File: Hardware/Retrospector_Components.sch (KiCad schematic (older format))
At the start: 122 parts, among them J1 SWD_Header, J2 Eurorack_10_pin_power, J3 Conn_01x08_Male, J4 Conn_01x08_Male, J5 Conn_01x08_Male, J6 Conn_01x08_Male, J7 USB_B_Micro, U1 STM32H743ZITx, U2 IS42S16400J-xC, U3 PCM5100APW, U4 SSI2164, U5 MCP6004, U6 MCP6004, U7 TL074, U8 LM1117-3.3, Y1 8MHz 20pF

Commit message: Final changes to PCBs for manufacture
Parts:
- added C53: 10uF, Capacitors_SMD:C_0805, symbol Device:C_Small
- C31, C33, C4, C6: footprint Capacitors_SMD:C_0805 -> Capacitors_SMD:C_0603_HandSoldering; Part_Number C49217 -> C23630
- C36: Rotation (none) -> 270
- C39, C40: footprint Capacitors_SMD:CP_Elec_5x5.3 -> Capacitors_SMD:CP_Elec_6.3x5.3; Part_Number (none) -> C249771
- C41: footprint Capacitors_SMD:CP_Elec_5x5.3 -> Capacitors_SMD:CP_Elec_6.3x7.7; Part_Number C134798 -> C108053; Rotation (none) -> 270
- D2, U8: Rotation (none) -> 90
- U1, U3: Rotation (none) -> 180
- Y1: footprint Crystals:Crystal_SMD_0603-2pin_6.0x3.5mm_HandSoldering -> Crystals:Crystal_SMD_5032-2pin_5.0x3.2mm_HandSoldering; Part_Number (none) -> C115962
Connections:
- wire segments 581 -> 584
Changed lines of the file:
@@
 F 3 "http://www.ti.com/lit/ds/symlink/lm4040-n.pdf" H 4050 11850 50  0001 C CIN
 F 4 "C69316" H 4050 11850 50  0001 C CNN "Part_Number"
+F 5 "90" H 4050 11850 50  0001 C CNN "Rotation"
 	1    4050 11850
 	0    1    1    0
@@
 F 0 "C41" H 4750 10250 50  0000 C CNN
 F 1 "47uF" H 4750 10150 50  0000 C CNN
-F 2 "Capacitors_SMD:CP_Elec_5x5.3" H 4588 10100 50  0001 C CNN
+F 2 "Capacitors_SMD:CP_Elec_6.3x7.7" H 4588 10100 50  0001 C CNN
 F 3 "~" H 4550 10250 50  0001 C CNN
-F 4 "C134798" H 4550 10250 50  0001 C CNN "Part_Number"
+F 4 "C108053" H 4550 10250 50  0001 C CNN "Part_Number"
+F 5 "270" H 4550 10250 50  0001 C CNN "Rotation"
 	1    4550 10250
 	1    0    0    -1
@@
 F 3 "http://ww1.microchip.com/downloads/en/DeviceDoc/21733j.pdf" H 9850 2150 50  0001 C CNN
 F 4 "C7378" H 9800 1950 50  0001 C CNN "Part_Number"
+F 5 "" H 9800 1950 50  0001 C CNN "Rotation"
 	1    9800 1950
 	1    0    0    1
@@
 F 0 "C39" V 1795 10000 50  0000 C CNN
 F 1 "22uF" V 1886 10000 50  0000 C CNN
-F 2 "Capacitors_SMD:CP_Elec_5x5.3" H 2088 9850 50  0001 C CNN
+F 2 "Capacitors_SMD:CP_Elec_6.3x5.3" H 2088 9850 50  0001 C CNN
 F 3 "~" H 2050 10000 50  0001 C CNN
-F 4 "" H 2050 10000 50  0001 C CNN "Part_Number"
+F 4 "C249771" H 2050 10000 50  0001 C CNN "Part_Number"
 	1    2050 10000
 	0    1    1    0
@@
 F 0 "C40" V 2305 11300 50  0000 C CNN
 F 1 "22uF" V 2214 11300 50  0000 C CNN
-F 2 "Capacitors_SMD:CP_Elec_5x5.3" H 2088 11150 50  0001 C CNN
+F 2 "Capacitors_SMD:CP_Elec_6.3x5.3" H 2088 11150 50  0001 C CNN
 F 3 "~" H 2050 11300 50  0001 C CNN
-F 4 "" H 2050 11300 50  0001 C CNN "Part_Number"
+F 4 "C249771" H 2050 11300 50  0001 C CNN "Part_Number"
 	1    2050 11300
 	0    -1   -1   0
@@
 F 3 "http://www.ti.com/lit/ds/symlink/lm1117.pdf" H 4050 10050 50  0001 C CNN
 F 4 "C6186" H 4050 10050 50  0001 C CNN "Part_Number"
+F 5 "90" H 4050 10050 50  0001 C CNN "Rotation"
 	1    4050 10050
 	1    0    0    -1
@@
 F 3 "https://lcsc.com/product-detail/Aluminum-Electrolytic-Capacitors-SMD_Lelon-VE-100M1HTR-0505_C249452.html/?href=jlc-SMT" H 3650 10250 50  0001 C CNN
 F 4 "C249452" H 3650 10250 50  0001 C CNN "Part_Number"
+F 5 "270" H 3650 10250 50  0001 C CNN "Rotation"
 	1    3650 10250
 	1    0    0    -1
@@
 F 0 "C6" V 1450 2350 50  0000 C CNN
 F 1 "2.2uF" V 1450 2600 50  0000 C CNN
-F 2 "Capacitors_SMD:C_0805" H 1500 2450 50  0001 C CNN
+F 2 "Capacitors_SMD:C_0603_HandSoldering" H 1500 2450 50  0001 C CNN
 F 3 "~" H 1500 2450 50  0001 C CNN
-F 4 "C49217" H 1500 2450 50  0001 C CNN "Part_Number"
+F 4 "C23630" H 1500 2450 50  0001 C CNN "Part_Number"
 	1    1500 2450
 	0    1    1    0
@@
 F 0 "C4" V 1250 2450 50  0000 C CNN
 F 1 "2.2uF" V 1250 2700 50  0000 C CNN
-F 2 "Capacitors_SMD:C_0805" H 1200 2550 50  0001 C CNN
+F 2 "Capacitors_SMD:C_0603_HandSoldering" H 1200 2550 50  0001 C CNN
 F 3 "~" H 1200 2550 50  0001 C CNN
-F 4 "C49217" H 1200 2550 50  0001 C CNN "Part_Number"
+F 4 "C23630" H 1200 2550 50  0001 C CNN "Part_Number"
 	1    1200 2550
 	0    1    1    0
@@
 F 0 "Y1" V 1600 3200 50  0000 R CNN
 F 1 "8MHz 20pF" V 1700 3400 50  0000 R CNN
-F 2 "Crystals:Crystal_SMD_0603-2pin_6.0x3.5mm_HandSoldering" H 1500 3300 50  0001 C CNN
+F 2 "Crystals:Crystal_SMD_5032-2pin_5.0x3.2mm_HandSoldering" H 1500 3300 50  0001 C CNN
 F 3 "~" H 1500 3300 50  0001 C CNN
+F 4 "C115962" H 1500 3300 50  0001 C CNN "Part_Number"
 	1    1500 3300
 	0    -1   -1   0
@@
 F 3 "http://www.ti.com/lit/ds/symlink/pcm5100.pdf" H 10450 10650 50  0001 C CNN
 F 4 "C131154" H 10500 9900 50  0001 C CNN "Part_Number"
+F 5 "180" H 10500 9900 50  0001 C CNN "Rotation"
 	1    10500 9900
 	1    0    0    -1
@@
 F 0 "C33" H 11265 10596 50  0000 L CNN
 F 1 "2.2uF" H 11265 10505 50  0000 L CNN
-F 2 "Capacitors_SMD:C_0805" H 11188 10400 50  0001 C CNN
+F 2 "Capacitors_SMD:C_0603_HandSoldering" H 11188 10400 50  0001 C CNN
 F 3 "~" H 11150 10550 50  0001 C CNN
-F 4 "C49217" H 11150 10550 50  0001 C CNN "Part_Number"
+F 4 "C23630" H 11150 10550 50  0001 C CNN "Part_Number"
 	1    11150 10550
 	1    0    0    -1
@@
 F 0 "C31" H 11265 9996 50  0000 L CNN
 F 1 "2.2uF" H 11265 9905 50  0000 L CNN
-F 2 "Capacitors_SMD:C_0805" H 11188 9800 50  0001 C CNN
+F 2 "Capacitors_SMD:C_0603_HandSoldering" H 11188 9800 50  0001 C CNN
 F 3 "~" H 11150 9950 50  0001 C CNN
-F 4 "C49217" H 11150 9950 50  0001 C CNN "Part_Number"
+F 4 "C23630" H 11150 9950 50  0001 C CNN "Part_Number"
 	1    11150 9950
 	1    0    0    -1
@@
 F 3 "http://www.st.com/st-web-ui/static/active/en/resource/technical/document/datasheet/DM00387108.pdf" H 3050 5250 50  0001 C CNN
 F 4 "C114408" H 3050 5250 50  0001 C CNN "Part_Number"
+F 5 "180" H 3050 5250 50  0001 C CNN "Rotation"
 	1    3050 5250
 	1    0    0    -1
@@
 	1    0    0    -1
 $EndComp
+$Comp
+L Device:C_Small C53
+U 1 1 5F91DB5F
+P 6050 10050
+F 0 "C53" H 5850 10150 50  0000 L CNN
+F 1 "10uF" H 5800 9950 50  0000 L CNN
+F 2 "Capacitors_SMD:C_0805" H 6088 9900 50  0001 C CNN
+F 3 "~" H 6050 10050 50  0001 C CNN
+F 4 "C15850 " H 6050 10050 50  0001 C CNN "Part_Number"
+	1    6050 10050
+	1    0    0    -1
+$EndComp
+Wire Wire Line
+	6050 9950 6250 9950
+Connection ~ 6250 9950
+Wire Wire Line
+	6050 10150 6050 10550
+Wire Wire Line
+	6050 10550 6250 10550
+Connection ~ 6250 10550
 $EndSCHEMATC

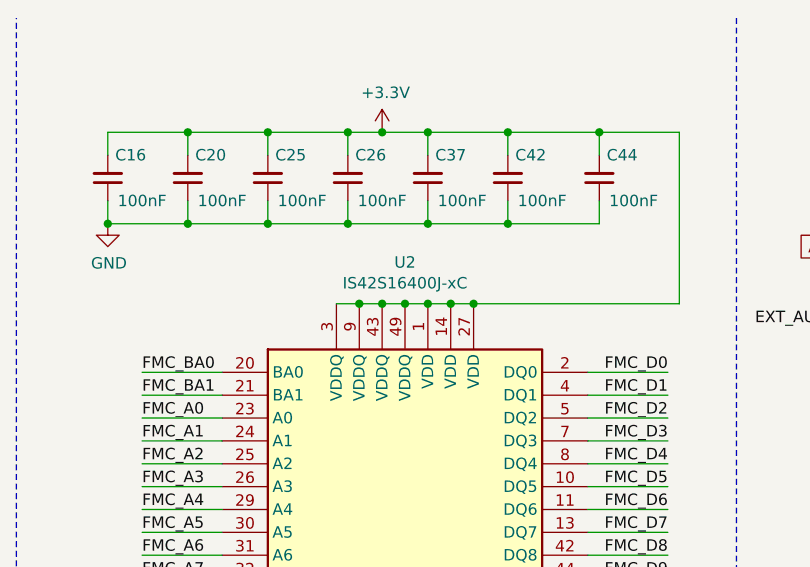
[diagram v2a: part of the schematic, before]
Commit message: Reduced clock speed; started implementing SDRAM code; ADC updates
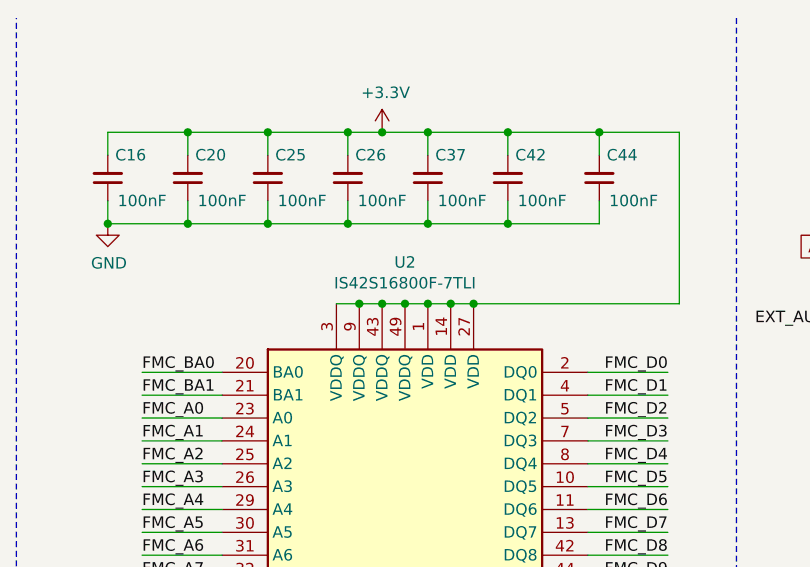
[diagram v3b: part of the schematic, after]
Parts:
- U2: value IS42S16400J-xC -> IS42S16800F-7TLI
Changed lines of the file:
@@
 P 6950 3150
 F 0 "U2" H 6950 4731 50  0000 C CNN
-F 1 "IS42S16400J-xC" H 6950 4640 50  0000 C CNN
+F 1 "IS42S16800F-7TLI" H 6950 4640 50  0000 C CNN
 F 2 "Custom_Footprints:TSOP-II-54_22.2x10.16mm_P0.8mm" H 6950 3150 50  0001 C CNN
-F 3 "http://www.issi.com/WW/pdf/42-45S16400J.pdf" H 6350 4400 50  0001 C CNN
+F 3 "https://lcsc.com/product-detail/DDR_ISSI-Integrated-Silicon-Solution-IS42S16800F-7TLI_C69411.html" H 6350 4400 50  0001 C CNN
 F 4 "C69411" H 6950 3150 50  0001 C CNN "Part_Number"
 	1    6950 3150

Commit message: Started updating schematics and pcb layout for rev 2 changes; updated and tested clock pin to use production assignment
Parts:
- removed C38: 100nF, Capacitors_SMD:C_0603_HandSoldering, symbol Device:C
- removed R22: 2k2, Resistors_SMD:R_0603_HandSoldering, symbol Device:R
- removed R42, R43: 1k, Resistors_SMD:R_0603_HandSoldering, symbol Device:R
- removed U8: LM1117-3.3, TO_SOT_Packages_SMD:SOT-223, symbol Regulator_Linear:LM1117-3.3
- added C38: 100nF, Capacitors_SMD:C_0603_HandSoldering, symbol Device:C_Small
- added C54, C55: 22uF, Capacitors_SMD:CP_Elec_4x5.8, symbol Device:C
- added C56: 10nF, Capacitors_SMD:C_0603_HandSoldering, symbol Device:C_Small
- added R22: 2k2, Resistors_SMD:R_0603_HandSoldering, symbol Device:R_Small
- added R43: 100R, Resistors_SMD:R_0603_HandSoldering, symbol Device:R_Small
- added TP? (x2): TestPoint, Custom_Footprints:1.3mm_Test_Point, symbol Connector:TestPoint
- added U8: NCV1117DT33T5G, TO_SOT_Packages_SMD:TO-252-2_Rectifier, symbol LDO_DPAK:NCV1117DT33T5G
- added U9: BA7807FP-E2, TO_SOT_Packages_SMD:TO-252-2_Rectifier, symbol LDO_DPAK:BA7807FP-E2
- C36: value 10uF -> 22uF; footprint Capacitors_SMD:CP_Elec_3x5.3 -> Capacitors_SMD:CP_Elec_4x5.8; Part_Number C249452 -> C178597; Rotation 270 -> (none)
- C39, C40: footprint Capacitors_SMD:CP_Elec_6.3x5.3 -> Capacitors_SMD:CP_Elec_4x5.8; Part_Number C249771 -> C178597
- C41: value 47uF -> 22uF; footprint Capacitors_SMD:CP_Elec_6.3x7.7 -> Capacitors_SMD:CP_Elec_4x5.8; Part_Number C108053 -> C178597; Rotation 270 -> (none)
- TP1, TP2, TP3, TP4, TP5, TP6: footprint Measurement_Points:Test_Point_Keystone_5005-5009_Compact -> Custom_Footprints:1.3mm_Test_Point
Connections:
- net labels added: +7V
- wire segments 584 -> 599
- no-connect marks 64 -> 63
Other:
- note added: "FIXME - resistors R42/43 are redundant??"
- moved on the sheet: C36, C39, C40, C41, C53, D2, D3, D4, J2, L1, TP1, TP2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

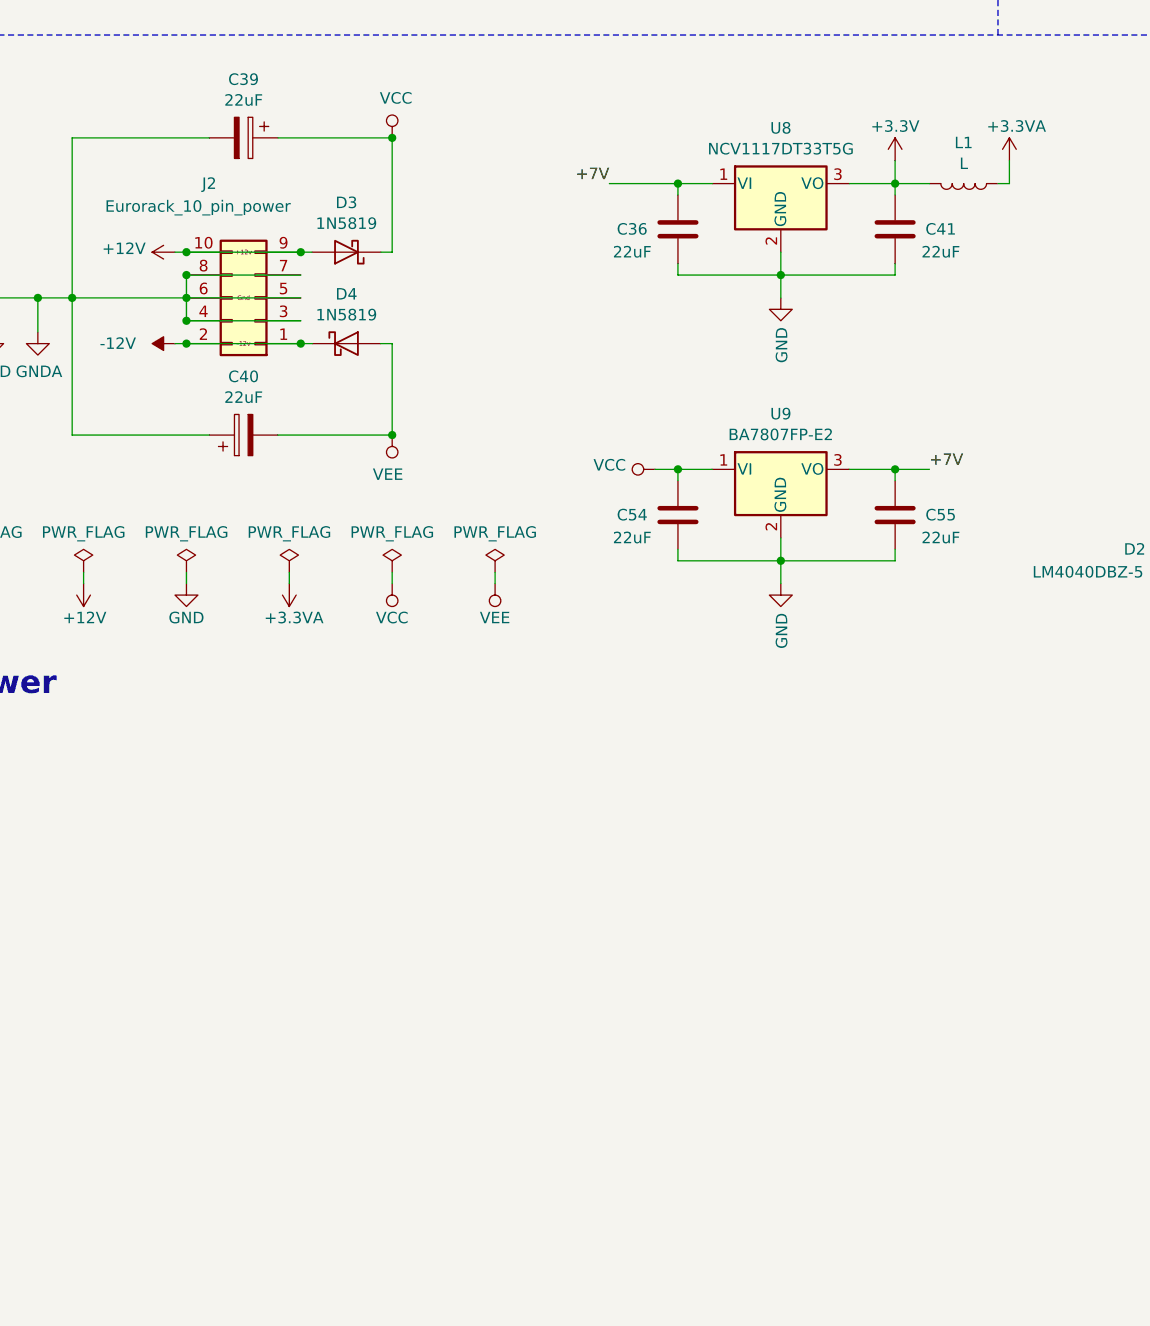
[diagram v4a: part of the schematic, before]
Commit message: Started adding circuitry for Buck conversion
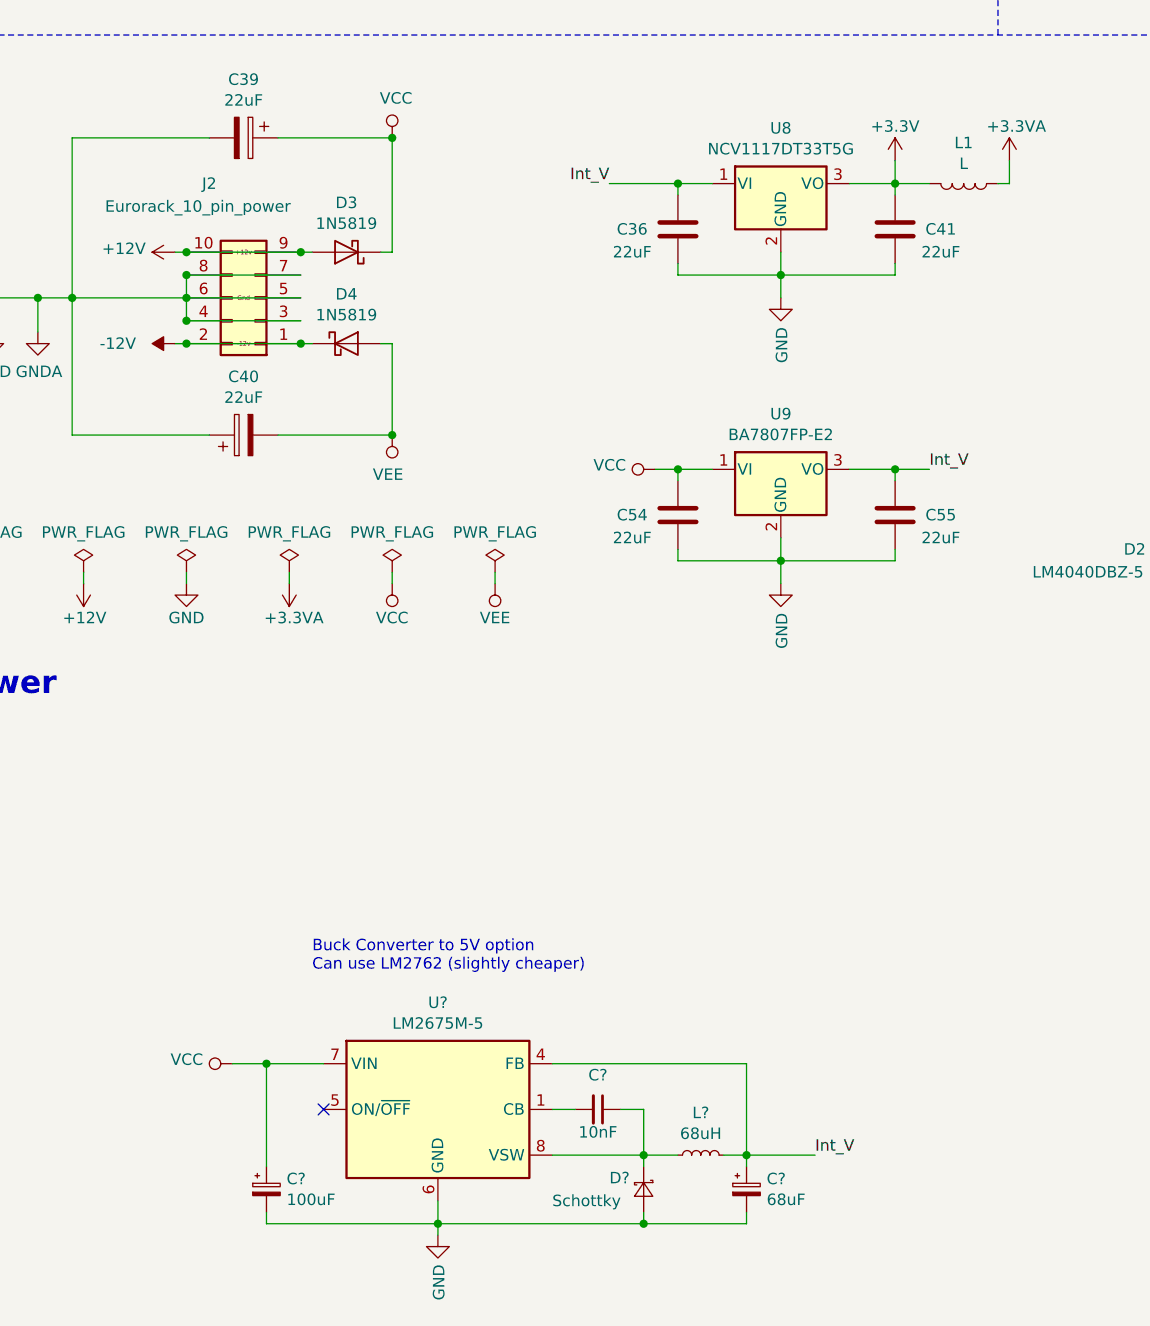
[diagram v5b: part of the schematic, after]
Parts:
- added C?: 10nF, Capacitors_SMD:C_0603_HandSoldering, symbol Device:C_Small
- added C?: 68uF, symbol Device:CP_Small
- added C?: 100uF, symbol Device:CP_Small
- added D?: Schottky, symbol Device:D_Schottky_Small
- added L?: 68uH, symbol Device:L_Small
- added U?: LM2675M-5, Housings_SOIC:SOIC-8_3.9x4.9mm_Pitch1.27mm, symbol Regulator_Switching:LM2675M-5
- C56: Part_Number (none) -> C57112
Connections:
- net GND: now also C?.2, C?.2, D?.2 (A), U?.6 (GND)
- net VCC: now also C?.1, U?.7 (VIN)
- net +7V renamed Int_V
- net Int_V: now also C?.1, L?.2, U?.4 (FB)
- new net: C?.2, U?.1 (CB)
- new net: C?.1, D?.1 (K), L?.1, U?.8 (VSW)
- no-connect marks 63 -> 64
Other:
- note added: "Buck Converter to 5V option\nCan use LM2762 (slightly cheaper)"
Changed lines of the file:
@@
 F 2 "Capacitors_SMD:C_0603_HandSoldering" H 14850 10500 50  0001 C CNN
 F 3 "~" H 14850 10500 50  0001 C CNN
-F 4 "" H 14850 10500 50  0001 C CNN "Part_Number"
+F 4 "C57112" H 14850 10500 50  0001 C CNN "Part_Number"
 	1    14850 10500
 	1    0    0    -1
@@
 Wire Wire Line
 	4300 11750 4800 11750
-Text Label 4950 11350 0    50   ~ 0
-+7V
-Text Label 3550 10100 2    50   ~ 0
-+7V
 Wire Wire Line
 	14050 10650 14050 10550
@@
 Wire Wire Line
 	7750 12250 7800 12250
+$Comp
+L Regulator_Switching:LM2675M-5 U?
+U 1 1 6DAC0E92
+P 2800 14150
+F 0 "U?" H 2800 14617 50  0000 C CNN
+F 1 "LM2675M-5" H 2800 14526 50  0000 C CNN
+F 2 "Housings_SOIC:SOIC-8_3.9x4.9mm_Pitch1.27mm" H 2850 13800 50  0001 L CIN
+F 3 "http://www.ti.com/lit/ds/symlink/lm2675.pdf" H 2800 14150 50  0001 C CNN
+F 4 "C180371" H 2800 14150 50  0001 C CNN "Part_Number"
+	1    2800 14150
+	1    0    0    -1
+$EndComp
+NoConn ~ 2300 14150
+$Comp
+L power:VCC #PWR?
+U 1 1 6DB2F14A
+P 1900 13950
+F 0 "#PWR?" H 1900 13800 50  0001 C CNN
+F 1 "VCC" V 1918 14077 50  0000 L CNN
+F 2 "" H 1900 13950 50  0001 C CNN
+F 3 "" H 1900 13950 50  0001 C CNN
+	1    1900 13950
+	0    -1   -1   0
+$EndComp
+$Comp
+L Device:D_Schottky_Small D?
+U 1 1 6DB2FC15
+P 3700 14500
+F 0 "D?" V 3650 14350 50  0000 L CNN
+F 1 "Schottky" V 3750 14100 50  0000 L CNN
+F 2 "" V 3700 14500 50  0001 C CNN
+F 3 "~" V 3700 14500 50  0001 C CNN
+	1    3700 14500
+	0    1    1    0
+$EndComp
+Wire Wire Line
+	3300 14350 3700 14350
+Wire Wire Line
+	3700 14350 3700 14400
+Wire Wire Line
+	2800 14550 2800 14650
+$Comp
+L Device:C_Small C?
+U 1 1 6DC7C12C
+P 3500 14150
+F 0 "C?" V 3350 14150 50  0000 C CNN
+F 1 "10nF" V 3600 14150 50  0000 C CNN
+F 2 "Capacitors_SMD:C_0603_HandSoldering" H 3500 14150 50  0001 C CNN
+F 3 "~" H 3500 14150 50  0001 C CNN
+F 4 "C57112" H 3500 14150 50  0001 C CNN "Part_Number"
+	1    3500 14150
+	0    1    1    0
+$EndComp
+Wire Wire Line
+	3300 14150 3400 14150
+Wire Wire Line
+	3600 14150 3700 14150
+Wire Wire Line
+	3700 14150 3700 14350
+Connection ~ 3700 14350
+$Comp
+L Device:CP_Small C?
+U 1 1 6DEA7A83
+P 4150 14500
+F 0 "C?" H 4238 14546 50  0000 L CNN
+F 1 "68uF" H 4238 14455 50  0000 L CNN
+F 2 "" H 4150 14500 50  0001 C CNN
+F 3 "~" H 4150 14500 50  0001 C CNN
+	1    4150 14500
+	1    0    0    -1
+$EndComp
+Wire Wire Line
+	3700 14350 3850 14350
+Wire Wire Line
+	4050 14350 4150 14350
+Wire Wire Line
+	4150 14350 4150 14400
+Wire Wire Line
+	4150 14650 4150 14600
+Connection ~ 2800 14650
+Wire Wire Line
+	2800 14700 2800 14650
+$Comp
+L power:GND #PWR?
+U 1 1 6DB2F5C6
+P 2800 14700
+F 0 "#PWR?" H 2800 14450 50  0001 C CNN
+F 1 "GND" V 2805 14572 50  0000 R CNN
+F 2 "" H 2800 14700 50  0001 C CNN
+F 3 "" H 2800 14700 50  0001 C CNN
+	1    2800 14700
+	1    0    0    -1
+$EndComp
+Wire Wire Line
+	4150 14350 4150 13950
+Wire Wire Line
+	4150 13950 3300 13950
+Connection ~ 4150 14350
+Wire Wire Line
+	4150 14350 4450 14350
+Text Label 4450 14350 0    50   ~ 0
+Int_V
+Text Label 4950 11350 0    50   ~ 0
+Int_V
+Text Label 3550 10100 2    50   ~ 0
+Int_V
+$Comp
+L Device:CP_Small C?
+U 1 1 6E46AC0A
+P 2050 14500
+F 0 "C?" H 2138 14546 50  0000 L CNN
+F 1 "100uF" H 2138 14455 50  0000 L CNN
+F 2 "" H 2050 14500 50  0001 C CNN
+F 3 "~" H 2050 14500 50  0001 C CNN
+	1    2050 14500
+	1    0    0    -1
+$EndComp
+Wire Wire Line
+	1900 13950 2050 13950
+Wire Wire Line
+	2050 13950 2050 14400
+Wire Wire Line
+	2050 13950 2300 13950
+Connection ~ 2050 13950
+Wire Wire Line
+	2050 14600 2050 14650
+Wire Wire Line
+	2050 14650 2800 14650
+Wire Wire Line
+	2800 14650 3700 14650
+Wire Wire Line
+	3700 14600 3700 14650
+Connection ~ 3700 14650
+Wire Wire Line
+	3700 14650 4150 14650
+Text Notes 2250 13550 0    50   ~ 0
+Buck Converter to 5V option\nCan use LM2762 (slightly cheaper)
+$Comp
+L Device:L_Small L?
+U 1 1 6DEA5F2E
+P 3950 14350
+F 0 "L?" V 4135 14350 50  0000 C CNN
+F 1 "68uH" V 4044 14350 50  0000 C CNN
+F 2 "" H 3950 14350 50  0001 C CNN
+F 3 "https://datasheet.lcsc.com/szlcsc/1912111437_3L-COILS-SNR6045K-680M_C326343.pdf" H 3950 14350 50  0001 C CNN
+F 4 "C326343" V 3950 14350 50  0001 C CNN "Part_Number"
+	1    3950 14350
+	0    -1   -1   0
+$EndComp
 $EndSCHEMATC
